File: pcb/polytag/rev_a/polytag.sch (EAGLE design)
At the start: 46 parts, among them J1 TC2030-JLINK-NL, J2 TC2030-JLINK-NL, J3 MICRO_USB_B_HIROSE_ZX62-B-5PA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, J4 BAT_HOLE, J5 BAT_HOLE, U1 NRF51822QF, U2 TRIPOINT, U3 LTC4065, U4 TPS715AXX, X1 EPSON-FA-128

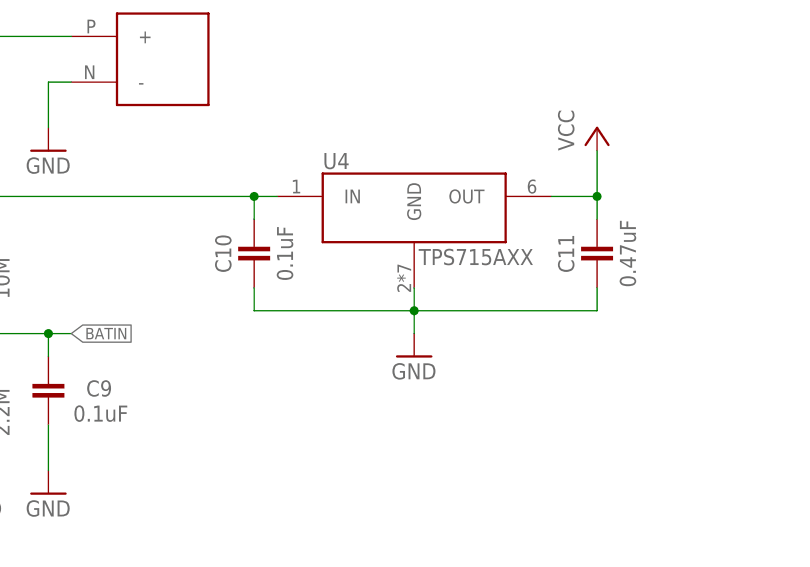
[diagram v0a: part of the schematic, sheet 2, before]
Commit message: fixed tenting problem
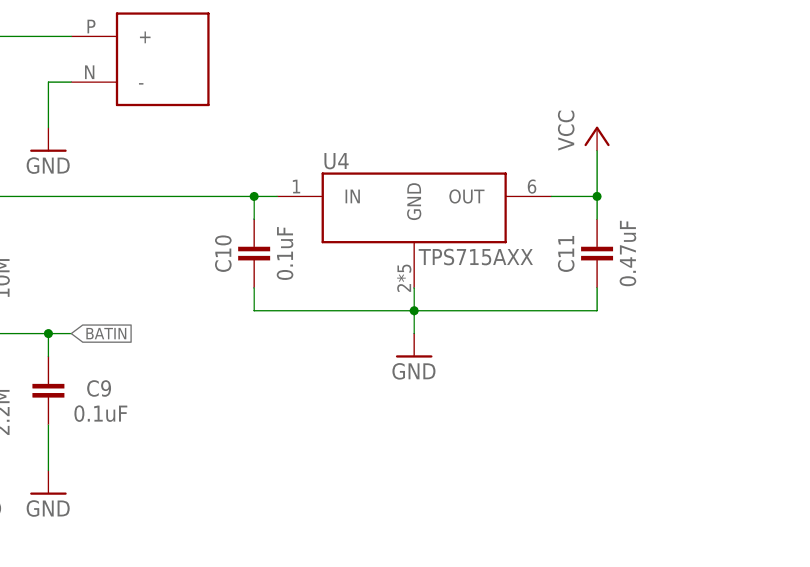
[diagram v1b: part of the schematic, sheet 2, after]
